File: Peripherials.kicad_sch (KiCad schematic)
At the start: 0 parts

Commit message: Schematic work 10/4
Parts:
- added C25, C28: 100n, symbol Device:C
- added C26, C27: 1u, symbol Device:C
- added D1, D2: D, Package_TO_SOT_SMD:SOT-666, symbol Device:D
- added J7, J8: USB_C_Receptacle_USB2.0_14P, symbol Connector:USB_C_Receptacle_USB2.0_14P
- added R10, R11, R14, R15: 5k1, Package_DIP:DIP-8_W7.62mm, symbol Device:R
- added R12, R13, R16, R17: 22R, Package_DIP:DIP-8_W7.62mm, symbol Device:R
- added U5, U6: USBLC6-2P6, Package_TO_SOT_SMD:SOT-666, symbol Power_Protection:USBLC6-2P6
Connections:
- new net: J8.A5 (CC1), R15.2
- new net: J8.B5 (CC2), R14.2
- new net: J7.A5 (CC1), R11.2
- new net: J7.B5 (CC2), R10.2
- new net ESP32_USB_D_N: U6.6 (I/O1)
- new net ESP32_USB_D_P: U6.4 (I/O2)
- new net GND: C25.2, C26.2, C27.2, C28.2, J7.A1 (GND), J7.A12 (GND), J7.B1 (GND), J7.B12 (GND), J8.A1 (GND), J8.A12 (GND), J8.B1 (GND), J8.B12 (GND), R10.1, R11.1, R14.1, R15.1, U5.2 (GND), U6.2 (GND)
- new net STM32_USB_D_N: U5.6 (I/O1)
- new net STM32_USB_D_P: U5.4 (I/O2)
- new net USB_5V: D1.1 (K), D2.1 (K)
- new net USB_D_N_ESD: R12.2, R16.2, U5.3 (I/O2), U6.3 (I/O2)
- new net USB_D_N_Resistor: J7.A7 (D-), J7.B7 (D-), J8.A7 (D-), J8.B7 (D-), R13.1, R17.1
- new net USB_D_P_ESD: R13.2, R17.2, U5.1 (I/O1), U6.1 (I/O1)
- new net USB_D_P_Resistor: J7.A6 (D+), J7.B6 (D+), J8.A6 (D+), J8.B6 (D+), R12.1, R16.1
- new net VBUS_ESP: C27.1, C28.1, D2.2 (A), J8.A4 (VBUS), J8.A9 (VBUS), J8.B4 (VBUS), J8.B9 (VBUS), U6.5 (VBUS)
- new net VBUS_STM: C25.1, C26.1, D1.2 (A), J7.A4 (VBUS), J7.A9 (VBUS), J7.B4 (VBUS), J7.B9 (VBUS), U5.5 (VBUS)
- no-connect marks 0 -> 2
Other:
- note added: "ESP32 USB-C"
- note added: "STM32 USB-C"
- note added: "USB-C PWR ORing"

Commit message: Small changes
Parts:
- added D3: D, Package_TO_SOT_SMD:SOT-666, symbol Device:D
- added J6: Conn_01x02_Pin, symbol Connector:Conn_01x02_Pin
- added Q1: NMOS, symbol Simulation_SPICE:NMOS
- added R22: 1R, Package_DIP:DIP-8_W7.62mm, symbol Device:R
- added R23: 10k, Package_DIP:DIP-8_W7.62mm, symbol Device:R
- added R24: 10R, Package_DIP:DIP-8_W7.62mm, symbol Device:R
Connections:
- net GND: now also R22.1, R23.1
- new net: Q1.2 (G), R23.2, R24.1
- new net: D3.2 (A), J6.1 (Pin_1), Q1.1 (D)
- new net: Q1.3 (S), R22.2
- new net +5V: D3.1 (K), J6.2 (Pin_2)
- new net FAN_PWM: R24.2
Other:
- note added: "5v 200mA"
- note added: "FAN PWM"
- note added: "Fan Part: https://www.adafruit.com/product/4468"

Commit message: MIsc
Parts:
- removed R22: 1R, Package_DIP:DIP-8_W7.62mm, symbol Device:R
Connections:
- net GND: now also Q1.3 (S)
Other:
- note added: "Connector 530470210"
- note added: "Fan 5v 200mA"
- note removed: "5v 200mA"
- moved on the sheet: C25, C26, C27, C28, D1, D2, D3, J6, J7, J8, Q1, R10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

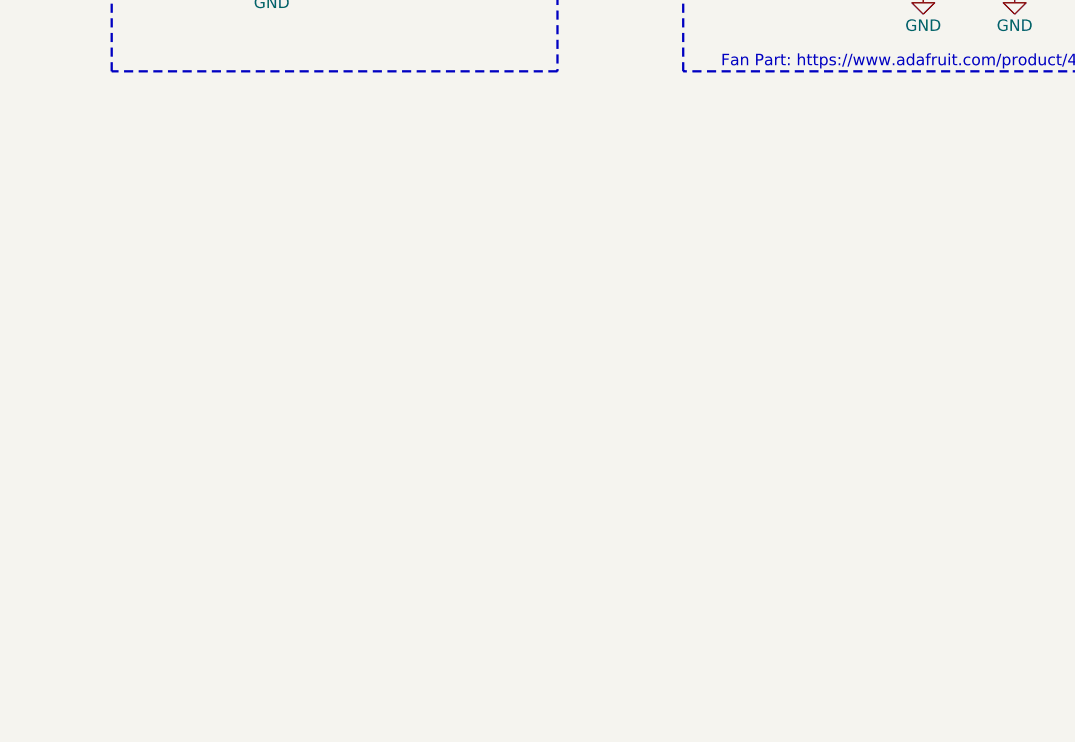
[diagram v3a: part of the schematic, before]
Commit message: added RTC
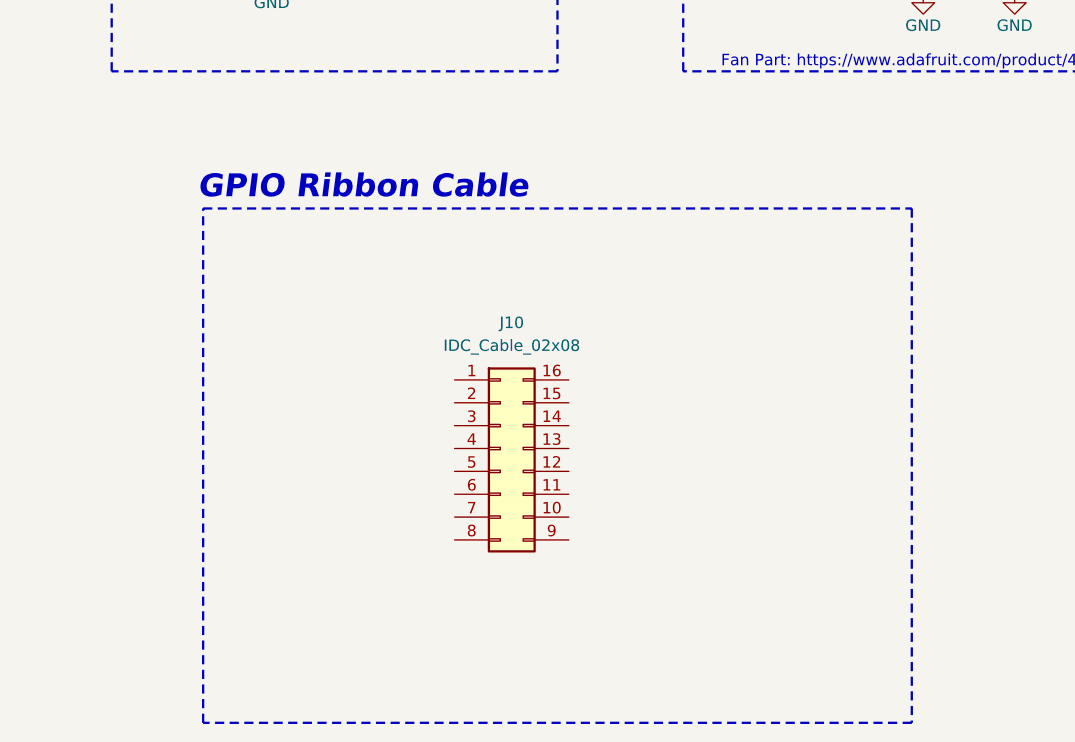
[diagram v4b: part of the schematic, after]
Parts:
- added J10: IDC_Cable_02x08, Connector_IDC:IDC-Header_2x08_P2.54mm_Vertical, symbol Connector_Generic:Conn_02x08_Counter_Clockwise
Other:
- note added: "GPIO Ribbon Cable"
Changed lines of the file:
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@@
+	)
+	(rectangle
+		(start 149.86 90.17)
+		(end 228.6 147.32)
+		(stroke
+			(width 0.254)
+			(type dash)
+			(color 0 0 0 1)
+		)
+		(fill
+			(type none)
+		)
 	)
 	(rectangle
@@
 		(exclude_from_sim no)
 		(at 164.846 15.748 0)
+		(effects
+			(font
+				(size 2.54 2.54)
+				(thickness 0.508)
+				(bold yes)
+				(italic yes)
+				(color 0 0 0 1)
+			)
+		)
+	)
+	(text "GPIO Ribbon Cable\n"
+		(exclude_from_sim no)
+		(at 167.64 87.884 0)
 		(effects
 			(font
@@
 					(unit 1)
 				)
+			)
+		)
+	)
+	(symbol
+		(lib_id "Connector_Generic:Conn_02x08_Counter_Clockwise")
+		(at 182.88 116.84 0)
+		(unit 1)
+		(body_style 1)
+		(exclude_from_sim no)
+		(in_bom yes)
+		(on_board yes)
+		(in_pos_files yes)
+		(dnp no)
+		(fields_autoplaced yes)
+		(property "Reference" "J10"
+			(at 184.15 102.87 0)
+			(show_name no)
+			(do_not_autoplace no)
+			(effects
+				(font
+					(size 1.27 1.27)
+				)
+			)
+		)
+		(property "Value" "IDC_Cable_02x08"
+			(at 184.15 105.41 0)
+			(show_name no)
+			(do_not_autoplace no)
+			(effects
+				(font
+					(size 1.27 1.27)
+				)
+			)
+		)
+		(property "Footprint" "Connector_IDC:IDC-Header_2x08_P2.54mm_Vertical"
+			(at 182.88 116.84 0)
+			(hide yes)
+			(show_name no)
+			(do_not_autoplace no)
+			(effects
+				(font
+					(size 1.27 1.27)
+				)
+			)
+		)
+		(property "Datasheet" ""
+			(at 182.88 116.84 0)
+			(hide yes)
+			(show_name no)
+			(do_not_autoplace no)
+			(effects
+				(font
+					(size 1.27 1.27)
+				)
+			)
+		)
+		(property "Description" "Generic connector, double row, 02x08, counter clockwise pin numbering scheme (similar to DIP package numbering), script generated (kicad-library-utils/schlib/autogen/connector/)"
+			(at 182.88 116.84 0)
+			(hide yes)
+			(show_name no)
+			(do_not_autoplace no)
+			(effects
+				(font
+					(size 1.27 1.27)
+				)
+			)
+		)
+		(pin "1"
+		)
+		(pin "2"
+		)
+		(pin "15"
+		)
+		(pin "16"
+		)
+		(pin "11"
+		)
+		(pin "12"
+		)
+		(pin "13"
+		)
+		(pin "14"
+		)
+		(pin "3"
+		)
+		(pin "4"
+		)
+		(pin "5"
+		)
+		(pin "6"
+		)
+		(pin "7"
+		)
+		(pin "8"
+		)
+		(pin "9"
+		)
+		(pin "10"
+		)
+		(instances
+			(project "SeniorDesign_PCB"
+				(path "/88e1ced0-9576-4565-ab29-f74bf51ccbda/c56479bc-1a8a-4e8e-8fbe-073cb4f795b5"
+					(reference "J10")
+					(unit 1)
+				)

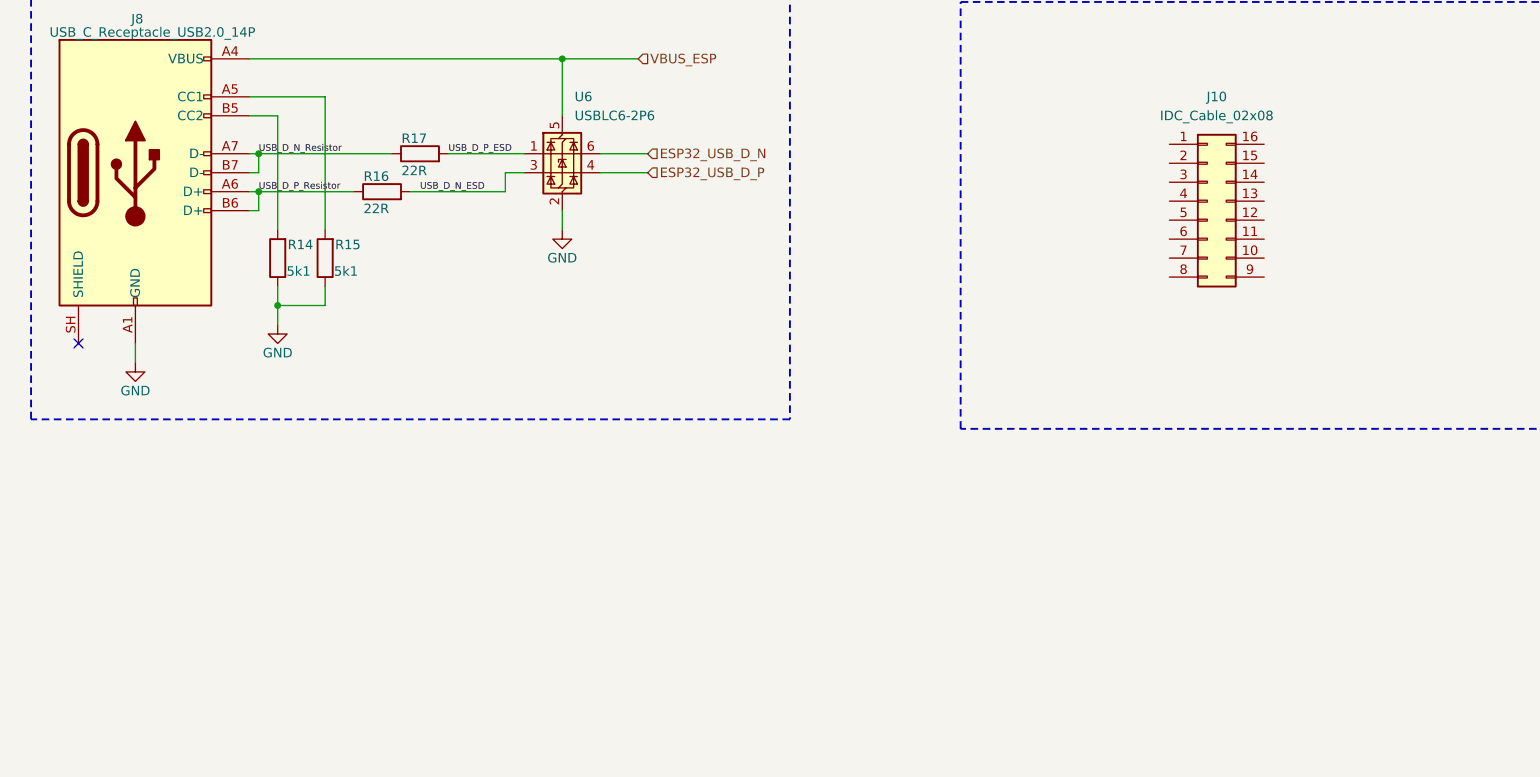
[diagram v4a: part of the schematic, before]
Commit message: added charge pump, fixed analog audio
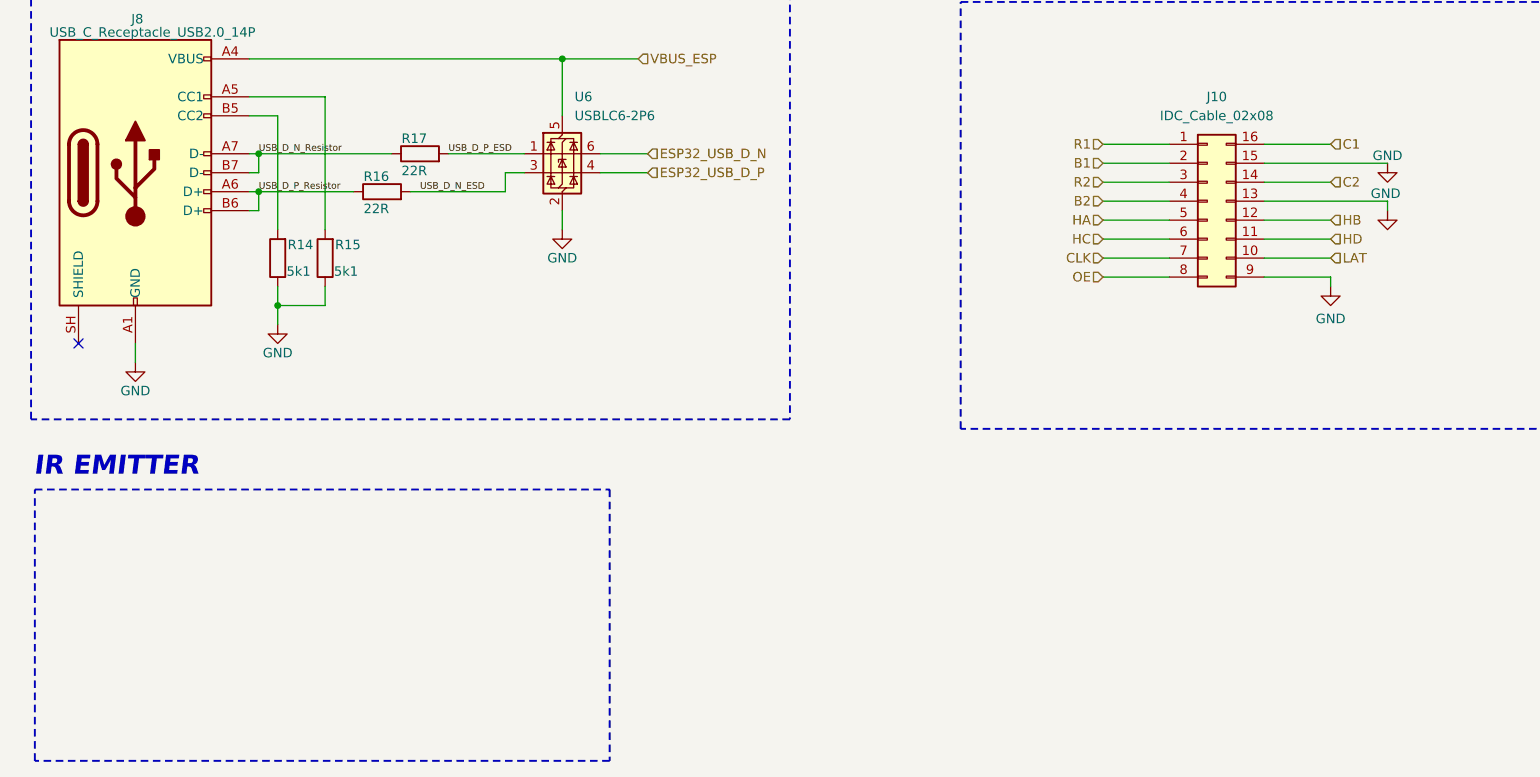
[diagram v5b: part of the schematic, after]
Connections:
- net GND: now also J10.13 (Pin_13), J10.15 (Pin_15), J10.9 (Pin_9)
- net R1: now reaches J10.1 (Pin_1)
- net LAT: now reaches J10.10 (Pin_10)
- net HD: now reaches J10.11 (Pin_11)
- net HB: now reaches J10.12 (Pin_12)
- net C2: now reaches J10.14 (Pin_14)
- net C1: now reaches J10.16 (Pin_16)
- net B1: now reaches J10.2 (Pin_2)
- net R2: now reaches J10.3 (Pin_3)
- net B2: now reaches J10.4 (Pin_4)
- net HA: now reaches J10.5 (Pin_5)
- net HC: now reaches J10.6 (Pin_6)
- net CLK: now reaches J10.7 (Pin_7)
- net OE: now reaches J10.8 (Pin_8)
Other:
- note added: "IR EMITTER"

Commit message: Minor tweaks
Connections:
- net B1 renamed MATRIX_B1
- net B2 renamed MATRIX_B2
- net C1 renamed MATRIX_G1
- net C2 renamed MATRIX_G2
- net CLK renamed MATRIX_CLK
- net HA renamed MATRIX_A
- net HB renamed MATRIX_B
- net HC renamed MATRIX_C
- net HD renamed MATRIX_D
- net LAT renamed MATRIX_LAT
- net OE renamed MATRIX_OE
- net R1 renamed MATRIX_R1
- net R2 renamed MATRIX_R2
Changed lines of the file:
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@@
+	)
+	(junction
+		(at 213.36 127)
+		(diameter 0)
+		(color 0 0 0 0)
 	)
 	(junction
@@
 	)
 	(junction
+		(at 213.36 116.84)
+		(diameter 0)
+		(color 0 0 0 0)
+	)
+	(junction
 		(at 58.42 130.81)
 		(diameter 0)
@@
 	(wire
 		(pts
+			(xy 213.36 111.76) (xy 213.36 116.84)
+		)
+		(stroke
+			(width 0)
+			(type default)
+		)
+	)
+	(wire
+		(pts
 			(xy 157.48 48.26) (xy 157.48 50.8)
 		)
@@
 	(wire
 		(pts
-			(xy 190.5 116.84) (xy 207.01 116.84)
+			(xy 190.5 116.84) (xy 213.36 116.84)
 		)
 		(stroke
@@
 	(wire
 		(pts
-			(xy 207.01 116.84) (xy 207.01 118.11)
+			(xy 213.36 116.84) (xy 213.36 127)
 		)
 		(stroke
@@
 	(wire
 		(pts
-			(xy 190.5 111.76) (xy 207.01 111.76)
+			(xy 190.5 111.76) (xy 213.36 111.76)
 		)
 		(stroke
@@
 	(wire
 		(pts
-			(xy 190.5 127) (xy 199.39 127)
+			(xy 190.5 127) (xy 213.36 127)
 		)
 		(stroke
@@
 	(wire
 		(pts
-			(xy 199.39 127) (xy 199.39 128.27)
+			(xy 213.36 127) (xy 213.36 128.27)
 		)
 		(stroke
@@
 		)
 	)
-	(hierarchical_label "HA"
+	(hierarchical_label "MATRIX_A"
 		(shape input)
 		(at 168.91 119.38 180)
@@
 		)
 	)
-	(hierarchical_label "R1"
+	(hierarchical_label "MATRIX_R1"
 		(shape input)
 		(at 168.91 109.22 180)
@@
 		)
 	)
-	(hierarchical_label "CLK"
+	(hierarchical_label "MATRIX_CLK"
 		(shape input)
 		(at 168.91 124.46 180)
@@
 		)
 	)
-	(hierarchical_label "HC"
+	(hierarchical_label "MATRIX_C"
 		(shape input)
 		(at 168.91 121.92 180)
@@
 		)
 	)
-	(hierarchical_label "C2"
+	(hierarchical_label "MATRIX_G2"
 		(shape input)
 		(at 199.39 114.3 0)
@@
 		)
 	)
-	(hierarchical_label "LAT"
+	(hierarchical_label "MATRIX_LAT"
 		(shape input)
 		(at 199.39 124.46 0)
@@
 		)
 	)
-	(hierarchical_label "B2"
+	(hierarchical_label "MATRIX_B2"
 		(shape input)
 		(at 168.91 116.84 180)
@@
 		)
 	)
-	(hierarchical_label "C1"
+	(hierarchical_label "MATRIX_G1"
 		(shape input)
 		(at 199.39 109.22 0)
@@
 		)
 	)
-	(hierarchical_label "HB"
+	(hierarchical_label "MATRIX_B"
 		(shape input)
 		(at 199.39 119.38 0)
@@
 		)
 	)
-	(hierarchical_label "HD"
+	(hierarchical_label "MATRIX_D"
 		(shape input)
 		(at 199.39 121.92 0)
@@
 		)
 	)
-	(hierarchical_label "R2"
+	(hierarchical_label "MATRIX_R2"
 		(shape input)
 		(at 168.91 114.3 180)
@@
 		)
 	)
-	(hierarchical_label "B1"
+	(hierarchical_label "MATRIX_B1"
 		(shape input)
 		(at 168.91 111.76 180)
@@
 		)
 	)
-	(hierarchical_label "OE"
+	(hierarchical_label "MATRIX_OE"
 		(shape input)
 		(at 168.91 127 180)
@@
 	)
 	(symbol
-		(lib_id "power:GND")
-		(at 207.01 118.11 0)
-		(unit 1)
-		(body_style 1)
-		(exclude_from_sim no)
-		(in_bom yes)
-		(on_board yes)
-		(in_pos_files yes)
-		(dnp no)
-		(property "Reference" "#PWR066"
-			(at 207.01 124.46 0)
-			(hide yes)
-			(show_name no)
-			(do_not_autoplace no)
-			(effects
-				(font
-					(size 1.27 1.27)
-				)
-			)
-		)
-		(property "Value" "GND"
-			(at 206.756 115.824 0)
-			(show_name no)
-			(do_not_autoplace no)
-			(effects
-				(font
-					(size 1.27 1.27)
-				)
-			)
-		)
-		(property "Footprint" ""
-			(at 207.01 118.11 0)
-			(hide yes)
-			(show_name no)
-			(do_not_autoplace no)
-			(effects
-				(font
-					(size 1.27 1.27)
-				)
-			)
-		)
-		(property "Datasheet" ""
-			(at 207.01 118.11 0)
-			(hide yes)
-			(show_name no)
-			(do_not_autoplace no)
-			(effects
-				(font
-					(size 1.27 1.27)
-				)
-			)
-		)
-		(property "Description" "Power symbol creates a global label with name \"GND\" , ground"
-			(at 207.01 118.11 0)
-			(hide yes)
-			(show_name no)
-			(do_not_autoplace no)
-			(effects
-				(font
-					(size 1.27 1.27)
-				)
-			)
-		)
-		(pin "1"
-		)
-		(instances
-			(project "SeniorDesign_PCB"
-				(path "/88e1ced0-9576-4565-ab29-f74bf51ccbda/c56479bc-1a8a-4e8e-8fbe-073cb4f795b5"
-					(reference "#PWR066")
-					(unit 1)
-				)
-			)
-		)
-	)
-	(symbol
 		(lib_id "Device:R")
 		(at 77.47 110.49 90)
@@
 	(symbol
 		(lib_id "power:GND")
-		(at 199.39 128.27 0)
+		(at 213.36 128.27 0)
 		(unit 1)
 		(body_style 1)
@@
 		(dnp no)
 		(property "Reference" "#PWR065"
-			(at 199.39 134.62 0)
+			(at 213.36 134.62 0)
 			(hide yes)
 			(show_name no)
@@
 		)
 		(property "Value" "GND"
-			(at 199.39 132.588 0)
+			(at 213.36 132.588 0)
 			(show_name no)
 			(do_not_autoplace no)
@@
 		)
 		(property "Footprint" ""
-			(at 199.39 128.27 0)
+			(at 213.36 128.27 0)
 			(hide yes)
 			(show_name no)
@@
 		)
 		(property "Datasheet" ""
-			(at 199.39 128.27 0)
+			(at 213.36 128.27 0)
 			(hide yes)
 			(show_name no)
@@
 		)
 		(property "Description" "Power symbol creates a global label with name \"GND\" , ground"
-			(at 199.39 128.27 0)
+			(at 213.36 128.27 0)
 			(hide yes)
 			(show_name no)
@@
 					(unit 1)
 				)
-			)
-		)
-	)
-	(symbol
-		(lib_id "power:GND")
-		(at 207.01 111.76 0)
-		(unit 1)
-		(body_style 1)
-		(exclude_from_sim no)
-		(in_bom yes)
-		(on_board yes)
-		(in_pos_files yes)
-		(dnp no)
-		(property "Reference" "#PWR067"
-			(at 207.01 118.11 0)
-			(hide yes)
-			(show_name no)
-			(do_not_autoplace no)
-			(effects
-				(font
-					(size 1.27 1.27)
-				)
-			)
-		)
-		(property "Value" "GND"
-			(at 207.01 110.744 0)
-			(show_name no)
-			(do_not_autoplace no)
-			(effects
-				(font
-					(size 1.27 1.27)
-				)
-			)
-		)
-		(property "Footprint" ""
-			(at 207.01 111.76 0)
-			(hide yes)
-			(show_name no)
-			(do_not_autoplace no)
-			(effects
-				(font
-					(size 1.27 1.27)
-				)
-			)
-		)
-		(property "Datasheet" ""
-			(at 207.01 111.76 0)
-			(hide yes)
-			(show_name no)
-			(do_not_autoplace no)
-			(effects
-				(font
-					(size 1.27 1.27)
-				)
-			)
-		)
-		(property "Description" "Power symbol creates a global label with name \"GND\" , ground"
-			(at 207.01 111.76 0)
-			(hide yes)
-			(show_name no)
-			(do_not_autoplace no)
-			(effects
-				(font
-					(size 1.27 1.27)
-				)
-			)
-		)
-		(pin "1"
-		)
-		(instances
-			(project "SeniorDesign_PCB"
-				(path "/88e1ced0-9576-4565-ab29-f74bf51ccbda/c56479bc-1a8a-4e8e-8fbe-073cb4f795b5"
-					(reference "#PWR067")
-					(unit 1)
-				)
